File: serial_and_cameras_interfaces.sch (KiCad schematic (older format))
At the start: 49 parts, among them J2 WE_68715014522, U5 NTS0102GT, U6 PCA9547BS

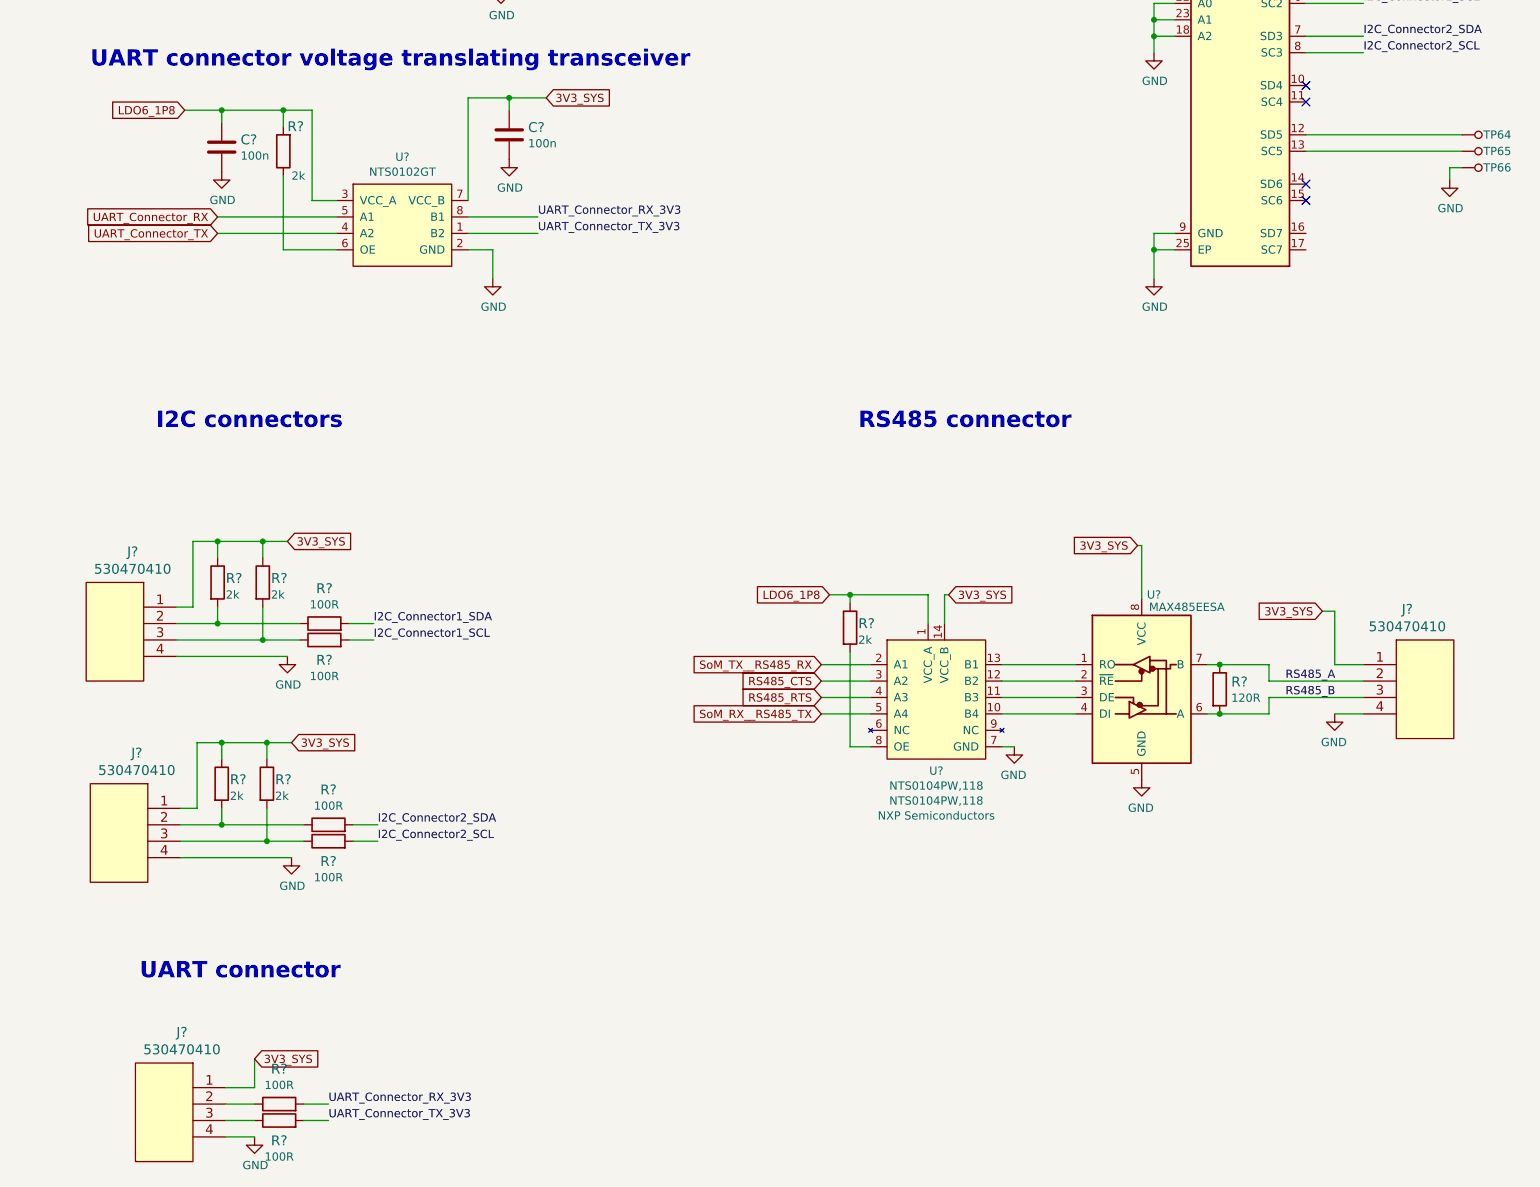
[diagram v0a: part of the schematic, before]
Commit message: Added schema for serial interface connectors
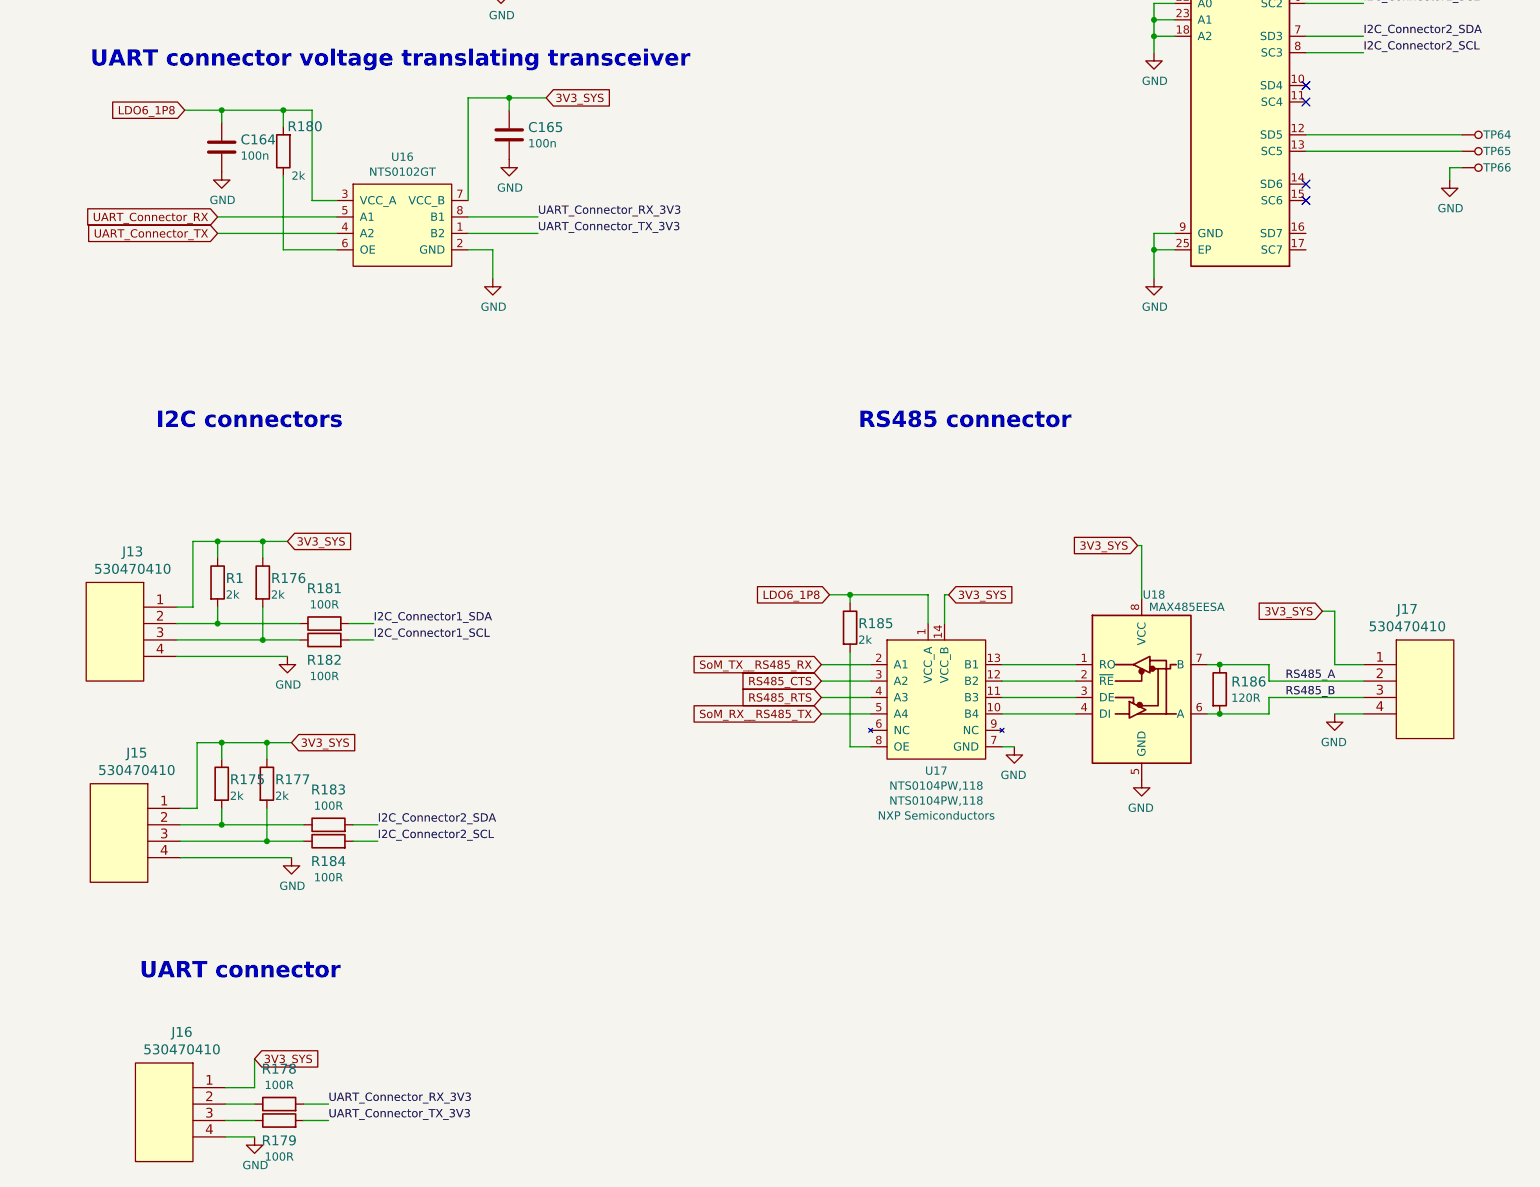
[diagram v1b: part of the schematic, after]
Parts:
- gave numbers to parts that had none: 22
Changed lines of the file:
@@
 I2C connectors\n
 $Comp
-L sc606-baseboard:R_2k_0402 R?
+L sc606-baseboard:R_2k_0402 R1
 U 1 1 626010A7
 P 2150 7250
-F 0 "R?" V 2125 7300 60  0000 L CNN
+F 0 "R1" V 2125 7300 60  0000 L CNN
 F 1 "R_2k_0402" H 2150 7100 60  0001 C CNN
 F 2 "sc606-baseboard-footprints:0402-res" H 2350 7450 60  0001 L CNN
@@
 $EndComp
 $Comp
-L sc606-baseboard:R_2k_0402 R?
+L sc606-baseboard:R_2k_0402 R176
 U 1 1 626010B0
 P 2425 7250
-F 0 "R?" V 2400 7300 60  0000 L CNN
+F 0 "R176" V 2400 7300 60  0000 L CNN
 F 1 "R_2k_0402" H 2425 7100 60  0001 C CNN
 F 2 "sc606-baseboard-footprints:0402-res" H 2625 7450 60  0001 L CNN
@@
 3V3_SYS
 $Comp
-L sc606-baseboard:GND #PWR?
+L sc606-baseboard:GND #PWR0172
 U 1 1 62626439
 P 2575 7700
-F 0 "#PWR?" H 2575 7450 50  0001 C CNN
+F 0 "#PWR0172" H 2575 7450 50  0001 C CNN
 F 1 "GND" H 2580 7527 50  0000 C CNN
 F 2 "" H 2575 7700 50  0001 C CNN
@@
 	2425 7000 2150 7000
 $Comp
-L sc606-baseboard:R_2k_0402 R?
+L sc606-baseboard:R_2k_0402 R175
 U 1 1 626C4A73
 P 2175 8475
-F 0 "R?" V 2150 8525 60  0000 L CNN
+F 0 "R175" V 2150 8525 60  0000 L CNN
 F 1 "R_2k_0402" H 2175 8325 60  0001 C CNN
 F 2 "sc606-baseboard-footprints:0402-res" H 2375 8675 60  0001 L CNN
@@
 $EndComp
 $Comp
-L sc606-baseboard:R_2k_0402 R?
+L sc606-baseboard:R_2k_0402 R177
 U 1 1 626C4A7C
 P 2450 8475
-F 0 "R?" V 2425 8525 60  0000 L CNN
+F 0 "R177" V 2425 8525 60  0000 L CNN
 F 1 "R_2k_0402" H 2450 8325 60  0001 C CNN
 F 2 "sc606-baseboard-footprints:0402-res" H 2650 8675 60  0001 L CNN
@@
 3V3_SYS
 $Comp
-L sc606-baseboard:GND #PWR?
+L sc606-baseboard:GND #PWR0179
 U 1 1 626C4A83
 P 2600 8925
-F 0 "#PWR?" H 2600 8675 50  0001 C CNN
+F 0 "#PWR0179" H 2600 8675 50  0001 C CNN
 F 1 "GND" H 2605 8752 50  0000 C CNN
 F 2 "" H 2600 8925 50  0001 C CNN
@@
 	2450 8225 2175 8225
 $Comp
-L sc606-baseboard:530470410 J?
+L sc606-baseboard:530470410 J13
 U 1 1 626F4EFF
 P 1900 7400
-F 0 "J?" H 2167 7737 60  0000 C CNN
+F 0 "J13" H 2167 7737 60  0000 C CNN
 F 1 "530470410" H 2167 7631 60  0000 C CNN
 F 2 "sc606-baseboard-footprints:530470410" H 2300 7140 60  0001 C CNN
@@
 	1900 7700 2575 7700
 $Comp
-L sc606-baseboard:530470410 J?
+L sc606-baseboard:530470410 J15
 U 1 1 627279FD
 P 1925 8625
-F 0 "J?" H 2192 8962 60  0000 C CNN
+F 0 "J15" H 2192 8962 60  0000 C CNN
 F 1 "530470410" H 2192 8856 60  0000 C CNN
 F 2 "sc606-baseboard-footprints:530470410" H 2325 8365 60  0001 C CNN
@@
 UART_Connector_RX
 $Comp
-L sc606-baseboard:530470410 J?
+L sc606-baseboard:530470410 J16
 U 1 1 627B87E5
 P 2200 10325
-F 0 "J?" H 2467 10662 60  0000 C CNN
+F 0 "J16" H 2467 10662 60  0000 C CNN
 F 1 "530470410" H 2467 10556 60  0000 C CNN
 F 2 "sc606-baseboard-footprints:530470410" H 2600 10065 60  0001 C CNN
@@
 3V3_SYS
 $Comp
-L sc606-baseboard:GND #PWR?
+L sc606-baseboard:GND #PWR0168
 U 1 1 627D6396
 P 2375 10625
-F 0 "#PWR?" H 2375 10375 50  0001 C CNN
+F 0 "#PWR0168" H 2375 10375 50  0001 C CNN
 F 1 "GND" H 2380 10452 50  0000 C CNN
 F 2 "" H 2375 10625 50  0001 C CNN
@@
 	2200 10325 2375 10325
 $Comp
-L sc606-baseboard:530470410 J?
+L sc606-baseboard:530470410 J17
 U 1 1 6280B1F3
 P 9125 7750
-F 0 "J?" H 9392 8087 60  0000 C CNN
+F 0 "J17" H 9392 8087 60  0000 C CNN
 F 1 "530470410" H 9392 7981 60  0000 C CNN
 F 2 "sc606-baseboard-footprints:530470410" H 9525 7490 60  0001 C CNN
@@
 $EndComp
 $Comp
-L sc606-baseboard:GND #PWR?
+L sc606-baseboard:GND #PWR0233
 U 1 1 62817A83
 P 8950 8050
-F 0 "#PWR?" H 8950 7800 50  0001 C CNN
+F 0 "#PWR0233" H 8950 7800 50  0001 C CNN
 F 1 "GND" H 8955 7877 50  0000 C CNN
 F 2 "" H 8950 8050 50  0001 C CNN
@@
 	9125 8050 8950 8050
 $Comp
-L sc606-baseboard:NTS0102GT U?
+L sc606-baseboard:NTS0102GT U16
 U 1 1 6283F680
 P 3275 5175
-F 0 "U?" H 3275 5690 50  0000 C CNN
+F 0 "U16" H 3275 5690 50  0000 C CNN
 F 1 "NTS0102GT" H 3275 5599 50  0000 C CNN
 F 2 "sc606-baseboard-footprints:PSON50P100X195X50-8N" H 3175 5675 50  0001 C CNN
@@
 UART connector voltage translating transceiver
 $Comp
-L sc606-baseboard:GND #PWR?
+L sc606-baseboard:GND #PWR0201
 U 1 1 62851A8A
 P 3825 5400
-F 0 "#PWR?" H 3825 5150 50  0001 C CNN
+F 0 "#PWR0201" H 3825 5150 50  0001 C CNN
 F 1 "GND" H 3830 5227 50  0000 C CNN
 F 2 "" H 3825 5400 50  0001 C CNN
@@
 	3675 4300 3675 4925
 $Comp
-L sc606-baseboard:C_100n_0402 C?
+L sc606-baseboard:C_100n_0402 C165
 U 1 1 628556E8
 P 3925 4525
-F 0 "C?" H 4040 4570 60  0000 L CNN
+F 0 "C165" H 4040 4570 60  0000 L CNN
 F 1 "C_100n_0402" H 3925 4375 60  0001 C CNN
 F 2 "sc606-baseboard-footprints:0402-cap" H 4125 4725 60  0001 L CNN
@@
 $EndComp
 $Comp
-L sc606-baseboard:GND #PWR?
+L sc606-baseboard:GND #PWR0227
 U 1 1 628556EE
 P 3925 4675
-F 0 "#PWR?" H 3925 4425 50  0001 C CNN
+F 0 "#PWR0227" H 3925 4425 50  0001 C CNN
 F 1 "GND" H 3930 4502 50  0000 C CNN
 F 2 "" H 3925 4675 50  0001 C CNN
@@
 	1950 4375 2175 4375
 $Comp
-L sc606-baseboard:C_100n_0402 C?
+L sc606-baseboard:C_100n_0402 C164
 U 1 1 6287D6F5
 P 2175 4600
-F 0 "C?" H 2290 4645 60  0000 L CNN
+F 0 "C164" H 2290 4645 60  0000 L CNN
 F 1 "C_100n_0402" H 2175 4450 60  0001 C CNN
 F 2 "sc606-baseboard-footprints:0402-cap" H 2375 4800 60  0001 L CNN
@@
 $EndComp
 $Comp
-L sc606-baseboard:GND #PWR?
+L sc606-baseboard:GND #PWR0137
 U 1 1 6287D6FB
 P 2175 4750
-F 0 "#PWR?" H 2175 4500 50  0001 C CNN
+F 0 "#PWR0137" H 2175 4500 50  0001 C CNN
 F 1 "GND" H 2180 4577 50  0000 C CNN
 F 2 "" H 2175 4750 50  0001 C CNN
@@
 	2175 4375 2550 4375
 $Comp
-L sc606-baseboard:R_2k_0402 R?
+L sc606-baseboard:R_2k_0402 R180
 U 1 1 62895A22
 P 2550 4625
-F 0 "R?" V 2700 4600 60  0000 R CNN
+F 0 "R180" V 2700 4600 60  0000 R CNN
 F 1 "R_2k_0402" H 2550 4475 60  0001 C CNN
 F 2 "sc606-baseboard-footprints:0402-res" H 2750 4825 60  0001 L CNN
@@
 	2375 10150 2375 10325
 $Comp
-L sc606-baseboard:R_100R_0402 R?
+L sc606-baseboard:R_100R_0402 R181
 U 1 1 62971F97
 P 2800 7500
-F 0 "R?" H 2800 7713 60  0000 C CNN
+F 0 "R181" H 2800 7713 60  0000 C CNN
 F 1 "R_100R_0402" H 2800 7350 60  0001 C CNN
 F 2 "sc606-baseboard-footprints:0402-res" H 3000 7700 60  0001 L CNN
@@
 $EndComp
 $Comp
-L sc606-baseboard:R_100R_0402 R?
+L sc606-baseboard:R_100R_0402 R182
 U 1 1 6298EF94
 P 2800 7600
-F 0 "R?" H 2800 7477 60  0000 C CNN
+F 0 "R182" H 2800 7477 60  0000 C CNN
 F 1 "R_100R_0402" H 2800 7450 60  0001 C CNN
 F 2 "sc606-baseboard-footprints:0402-res" H 3000 7800 60  0001 L CNN
@@
 $EndComp
 $Comp
-L sc606-baseboard:R_100R_0402 R?
+L sc606-baseboard:R_100R_0402 R183
 U 1 1 6299DD58
 P 2825 8725
-F 0 "R?" H 2825 8938 60  0000 C CNN
+F 0 "R183" H 2825 8938 60  0000 C CNN
 F 1 "R_100R_0402" H 2825 8575 60  0001 C CNN
 F 2 "sc606-baseboard-footprints:0402-res" H 3025 8925 60  0001 L CNN
@@
 $EndComp
 $Comp
-L sc606-baseboard:R_100R_0402 R?
+L sc606-baseboard:R_100R_0402 R184
 U 1 1 6299DD61
 P 2825 8825
-F 0 "R?" H 2825 8702 60  0000 C CNN
+F 0 "R184" H 2825 8702 60  0000 C CNN
 F 1 "R_100R_0402" H 2825 8675 60  0001 C CNN
 F 2 "sc606-baseboard-footprints:0402-res" H 3025 9025 60  0001 L CNN
@@
 	2975 8825 3125 8825
 $Comp
-L sc606-baseboard:R_100R_0402 R?
+L sc606-baseboard:R_100R_0402 R178
 U 1 1 629FF68B
 P 2525 10425
-F 0 "R?" H 2525 10638 60  0000 C CNN
+F 0 "R178" H 2525 10638 60  0000 C CNN
 F 1 "R_100R_0402" H 2525 10275 60  0001 C CNN
 F 2 "sc606-baseboard-footprints:0402-res" H 2725 10625 60  0001 L CNN
@@
 $EndComp
 $Comp
-L sc606-baseboard:R_100R_0402 R?
+L sc606-baseboard:R_100R_0402 R179
 U 1 1 629FF694
 P 2525 10525
-F 0 "R?" H 2525 10402 60  0000 C CNN
+F 0 "R179" H 2525 10402 60  0000 C CNN
 F 1 "R_100R_0402" H 2525 10375 60  0001 C CNN
 F 2 "sc606-baseboard-footprints:0402-res" H 2725 10725 60  0001 L CNN
@@
 	9125 7950 8550 7950
 $Comp
-L sc606-baseboard:MAX485EESA U?
+L sc606-baseboard:MAX485EESA U18
 U 1 1 6215F13F
 P 7775 7850
-F 0 "U?" H 7850 8375 50  0000 C CNN
+F 0 "U18" H 7850 8375 50  0000 C CNN
 F 1 "MAX485EESA" H 8050 8300 50  0000 C CNN
 F 2 "sc606-baseboard-footprints:SOIC-8_W3.9mm" H 8675 7100 50  0001 C CNN
@@
 $EndComp
 $Comp
-L sc606-baseboard:R_120R_0402 R?
+L sc606-baseboard:R_120R_0402 R186
 U 1 1 62160CC0
 P 8250 7900
-F 0 "R?" V 8205 7970 60  0000 L CNN
+F 0 "R186" V 8205 7970 60  0000 L CNN
 F 1 "R_120R_0402" H 8250 7750 60  0001 C CNN
 F 2 "sc606-baseboard-footprints:0402-res" H 8450 8100 60  0001 L CNN
@@
 	8250 8050 8550 8050
 $Comp
-L sc606-baseboard:GND #PWR?
+L sc606-baseboard:GND #PWR0232
 U 1 1 621CB438
 P 7775 8450
-F 0 "#PWR?" H 7775 8200 50  0001 C CNN
+F 0 "#PWR0232" H 7775 8200 50  0001 C CNN
 F 1 "GND" H 7780 8277 50  0000 C CNN
 F 2 "" H 7775 8450 50  0001 C CNN
@@
 RS485_CTS
 $Comp
-L sc606-baseboard:NTS0104PW,118 U?
+L sc606-baseboard:NTS0104PW,118 U17
 U 1 1 6229AA9A
 P 6525 7950
-F 0 "U?" H 6525 7503 50  0000 C CNN
+F 0 "U17" H 6525 7503 50  0000 C CNN
 F 1 "NTS0104PW,118" H 6525 7412 50  0000 C CNN
 F 2 "sc606-baseboard-footprints:TSSOP-14_W4.4mm" H 7575 8600 50  0001 C CNN
@@
 $EndComp
 $Comp
-L sc606-baseboard:GND #PWR?
+L sc606-baseboard:GND #PWR0231
 U 1 1 6229BEC9
 P 7000 8250
-F 0 "#PWR?" H 7000 8000 50  0001 C CNN
+F 0 "#PWR0231" H 7000 8000 50  0001 C CNN
 F 1 "GND" H 7005 8077 50  0000 C CNN
 F 2 "" H 7000 8250 50  0001 C CNN
@@
 	7775 7025 7750 7025
 $Comp
-L sc606-baseboard:R_2k_0402 R?
+L sc606-baseboard:R_2k_0402 R185
 U 1 1 6246A150
 P 6000 7525
-F 0 "R?" V 5975 7575 60  0000 L CNN
+F 0 "R185" V 5975 7575 60  0000 L CNN
 F 1 "R_2k_0402" H 6000 7375 60  0001 C CNN
 F 2 "sc606-baseboard-footprints:0402-res" H 6200 7725 60  0001 L CNN
